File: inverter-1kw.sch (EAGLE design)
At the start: 200 parts, among them IC1 LMV358MMX, IC2 LMV358MMX, U1 ACS712, U4 ACS712, U5 SI8230, U6 SI8230, U7 ACS712, X1 GMSTBV3, X2 MSTBV2

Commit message: Driver ve filtre devresi yerleşimleri yapıldı.
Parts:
- removed C33, C40: (no value), rcl:CPOL-EUE7.5-18
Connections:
- net AGND: no longer C33.-, C40.-
- net VSUPPLY+: no longer C33.+, C40.+

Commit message: Test padler eklendi. Kart destek noktalariyla toprak arasina kondansatorler eklendi.
Cin desarji icin kullanilacak direnc icin 4adet 1206 eklendi.
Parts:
- added C33, C40, C75, C76: 100n, rcl:C-EUC0805
- added R41, R42, R43: (no value), rcl:R-EU_R1206
- added R44: 0R, rcl:R-EU_R1206
- added TP1, TP17, TP18, TP2, TP3, TP4: TPTP17R, testpad:TPTP17R
- added TP10, TP11, TP12, TP13, TP14, TP15, TP16, TP19, TP20, TP21, TP22, TP23, TP24, TP25, TP26, TP27, TP28, TP29, TP30, TP31, TP32, TP33, TP34, TP5, TP6, TP7, TP8, TP9: TPTP06R, testpad:TPTP06R
- R28: device rcl:R-EU_0411/12 -> rcl:R-EU_R1206
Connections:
- new net N$40: C33.2, H1.MOUNT
- new net N$41: C40.2, H2.MOUNT
- new net N$42: C75.1, H3.MOUNT
- new net N$43: C76.1, H4.MOUNT
- new net SUPPLY+: R3.1
- net AGND: now also R41.1, R42.1, R43.1, R44.1, TP10.TP, TP3.TP, TP4.TP, TP9.TP
- net DGND: now also R44.2, TP15.TP, TP16.TP, TP26.TP, TP34.TP
- net G11_PWM: now also TP11.TP
- net G12_PWM: now also TP12.TP
- net G13_PWM: now also TP13.TP
- net G14_PWM: now also TP14.TP
- net IA_SENS: now also TP30.TP
- net IB_SENS: now also TP31.TP
- net IIN_SENS: now also TP33.TP
- net N$20: now also TP23.TP
- net N$23: now also TP24.TP
- net N$35: now also TP5.TP
- net N$37: now also TP7.TP
- net N$7: now also TP19.TP
- net N$75: now also TP6.TP
- net N$81: now also TP8.TP
- net N$9: now also TP20.TP
- net PE: now also C33.1, C40.1, C75.2, C76.2; no longer H1.MOUNT, H2.MOUNT, H3.MOUNT, H4.MOUNT
- net SW_LEG_A: now also TP1.TP, TP28.TP
- net SW_LEG_B: now also TP2.TP
- net VA_OUT: now also TP17.TP
- net VB_OUT: now also TP18.TP
- net VG1_M: now also TP29.TP
- net VG1_P: now also TP27.TP
- net VIN: no longer R3.1
- net VIN_SENS: now also TP32.TP
- net VIN_SENS_DIFF: now also TP21.TP
- net VOUT_SENS_DIFF: now also TP25.TP
- net VREF: now also TP22.TP
- net VSUPPLY+: now also R41.2, R42.2, R43.2

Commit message: bağlantıların bir kısmı yapıldı.
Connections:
- net +3V3: now also SV2.8; no longer SV2.7
- net AGND: now also X1-2.1; no longer X1-3.1
- net DGND: now also SV2.7; no longer SV2.8
- net VSUPPLY+: now also X1-3.1; no longer X1-2.1
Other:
- moved on the sheet: R96, X1-1, X1-2, X1-3
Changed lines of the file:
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@@
 <sheet>
 <plain>
-<wire x1="2.54" y1="-66.04" x2="259.08" y2="-66.04" width="0.6096" layer="125" style="longdash"/>
-<wire x1="259.08" y1="-66.04" x2="260.35" y2="-194.31" width="0.6096" layer="125" style="longdash"/>
+<wire x1="2.54" y1="-66.04" x2="260.35" y2="-66.04" width="0.6096" layer="125" style="longdash"/>
+<wire x1="260.35" y1="-66.04" x2="260.35" y2="-194.31" width="0.6096" layer="125" style="longdash"/>
 <wire x1="260.35" y1="-194.31" x2="3.81" y2="-194.31" width="0.6096" layer="125" style="longdash"/>
 <wire x1="3.81" y1="-194.31" x2="2.54" y2="-66.04" width="0.6096" layer="125" style="longdash"/>
@@
 <attribute name="VALUE" x="298.45" y="-128.27" size="1.778" layer="96" rot="R270"/>
 </instance>
-<instance part="+3V2" gate="G$1" x="300.99" y="-130.81" smashed="yes" rot="R180">
-<attribute name="VALUE" x="303.53" y="-125.73" size="1.778" layer="96" rot="R270"/>
+<instance part="+3V2" gate="G$1" x="303.53" y="-130.81" smashed="yes" rot="R180">
+<attribute name="VALUE" x="306.07" y="-125.73" size="1.778" layer="96" rot="R270"/>
 </instance>
-<instance part="SUPPLY8" gate="G$1" x="303.53" y="-129.54" smashed="yes">
-<attribute name="VALUE" x="300.863" y="-132.715" size="1.778" layer="96"/>
+<instance part="SUPPLY8" gate="G$1" x="300.99" y="-129.54" smashed="yes">
+<attribute name="VALUE" x="298.323" y="-132.715" size="1.778" layer="96"/>
 </instance>
 <instance part="U1" gate="U1" x="669.29" y="50.8" smashed="yes" rot="R90">
@@
 <attribute name="VALUE" x="127.762" y="234.95" size="1.778" layer="96" rot="R90"/>
 </instance>
-<instance part="R96" gate="G$1" x="124.46" y="218.44" smashed="yes" rot="R90">
-<attribute name="NAME" x="122.9614" y="214.63" size="1.778" layer="95" rot="R90"/>
-<attribute name="VALUE" x="127.762" y="214.63" size="1.778" layer="96" rot="R90"/>
+<instance part="R96" gate="G$1" x="124.46" y="217.17" smashed="yes" rot="R90">
+<attribute name="NAME" x="122.9614" y="213.36" size="1.778" layer="95" rot="R90"/>
+<attribute name="VALUE" x="127.762" y="213.36" size="1.778" layer="96" rot="R90"/>
 </instance>
 <instance part="AGND5" gate="VR1" x="746.76" y="71.12" smashed="yes" rot="R180">
@@
 <attribute name="VALUE" x="426.6438" y="-83.566" size="1.778" layer="96" rot="R90"/>
 </instance>
-<instance part="X1" gate="-1" x="6.35" y="-40.64" smashed="yes">
-<attribute name="NAME" x="1.27" y="-39.751" size="1.778" layer="95" rot="R180"/>
+<instance part="X1" gate="-1" x="8.89" y="-39.37" smashed="yes">
+<attribute name="NAME" x="3.81" y="-38.481" size="1.778" layer="95" rot="R180"/>
 </instance>
-<instance part="X1" gate="-2" x="6.35" y="368.3" smashed="yes">
-<attribute name="NAME" x="1.27" y="369.189" size="1.778" layer="95" rot="R180"/>
+<instance part="X1" gate="-2" x="8.89" y="-27.94" smashed="yes">
+<attribute name="NAME" x="3.81" y="-27.051" size="1.778" layer="95" rot="R180"/>
 </instance>
-<instance part="X1" gate="-3" x="6.35" y="-27.94" smashed="yes">
-<attribute name="NAME" x="1.016" y="-27.051" size="1.778" layer="95" rot="R180"/>
-<attribute name="VALUE" x="0" y="-31.75" size="1.778" layer="96"/>
+<instance part="X1" gate="-3" x="6.35" y="368.3" smashed="yes">
+<attribute name="NAME" x="1.016" y="369.189" size="1.778" layer="95" rot="R180"/>
+<attribute name="VALUE" x="0" y="364.49" size="1.778" layer="96"/>
 </instance>
 <instance part="X2" gate="-1" x="815.34" y="224.79" smashed="yes" rot="R180">
@@
 <attribute name="NAME" x="823.214" y="37.211" size="1.778" layer="95"/>
 </instance>
-<instance part="PE1" gate="M" x="13.97" y="-45.72" smashed="yes">
-<attribute name="VALUE" x="11.43" y="-48.26" size="1.778" layer="96" rot="R90"/>
+<instance part="PE1" gate="M" x="16.51" y="-44.45" smashed="yes">
+<attribute name="VALUE" x="13.97" y="-46.99" size="1.778" layer="96" rot="R90"/>
 </instance>
 <instance part="PE2" gate="M" x="414.02" y="-104.14" smashed="yes">
@@
 <segment>
 <pinref part="SUPPLY8" gate="G$1" pin="DGND"/>
-<wire x1="303.53" y1="-127" x2="303.53" y2="-116.84" width="0.1524" layer="91"/>
-<label x="303.53" y="-127" size="1.778" layer="95" rot="R90"/>
-<pinref part="SV2" gate="G$1" pin="8"/>
+<wire x1="300.99" y1="-127" x2="300.99" y2="-116.84" width="0.1524" layer="91"/>
+<label x="300.99" y="-127" size="1.778" layer="95" rot="R90"/>
+<pinref part="SV2" gate="G$1" pin="7"/>
 </segment>
 <segment>
@@
 <segment>
 <pinref part="+3V2" gate="G$1" pin="+3V3"/>
-<wire x1="300.99" y1="-128.27" x2="300.99" y2="-116.84" width="0.1524" layer="91"/>
-<label x="303.53" y="-130.81" size="1.778" layer="95" rot="R180"/>
-<pinref part="SV2" gate="G$1" pin="7"/>
-<label x="300.99" y="-127" size="1.778" layer="95" rot="R90"/>
+<wire x1="303.53" y1="-128.27" x2="303.53" y2="-116.84" width="0.1524" layer="91"/>
+<label x="306.07" y="-127" size="1.778" layer="95" rot="R90"/>
+<label x="303.53" y="-127" size="1.778" layer="95" rot="R90"/>
+<pinref part="SV2" gate="G$1" pin="8"/>
 </segment>
 <segment>
@@
 <junction x="48.26" y="-27.94"/>
 <wire x1="48.26" y1="173.99" x2="48.26" y2="-27.94" width="0.6096" layer="91"/>
-<wire x1="48.26" y1="-27.94" x2="11.43" y2="-27.94" width="0.6096" layer="91"/>
+<wire x1="48.26" y1="-27.94" x2="13.97" y2="-27.94" width="0.6096" layer="91"/>
 <pinref part="R96" gate="G$1" pin="1"/>
-<wire x1="124.46" y1="213.36" x2="124.46" y2="-27.94" width="0.1524" layer="91"/>
+<wire x1="124.46" y1="212.09" x2="124.46" y2="-27.94" width="0.1524" layer="91"/>
 <junction x="124.46" y="-27.94"/>
 <pinref part="LED5" gate="G$1" pin="C"/>
@@
 <pinref part="C48" gate="G$1" pin="2"/>
 <pinref part="C49" gate="G$1" pin="2"/>
-<pinref part="X1" gate="-3" pin="1"/>
 <pinref part="C28" gate="G$1" pin="2"/>
 <wire x1="72.39" y1="177.8" x2="72.39" y2="-27.94" width="0.6096" layer="91"/>
@@
 <wire x1="36.83" y1="173.99" x2="40.64" y2="173.99" width="0.1524" layer="91"/>
 <junction x="40.64" y="173.99"/>
+<pinref part="X1" gate="-2" pin="1"/>
 </segment>
 <segment>
@@
 <junction x="124.46" y="368.3"/>
 <wire x1="48.26" y1="186.69" x2="48.26" y2="187.96" width="0.1524" layer="91"/>
-<pinref part="X1" gate="-2" pin="1"/>
 <pinref part="C28" gate="G$1" pin="1"/>
 <wire x1="72.39" y1="185.42" x2="72.39" y2="368.3" width="0.6096" layer="91"/>
@@
 <wire x1="36.83" y1="189.23" x2="40.64" y2="189.23" width="0.1524" layer="91"/>
 <junction x="40.64" y="189.23"/>
+<pinref part="X1" gate="-3" pin="1"/>
 </segment>
 </net>
@@
 <pinref part="R96" gate="G$1" pin="2"/>
 <wire x1="124.46" y1="233.68" x2="124.46" y2="228.6" width="0.1524" layer="91"/>
-<wire x1="124.46" y1="228.6" x2="124.46" y2="223.52" width="0.1524" layer="91"/>
+<wire x1="124.46" y1="228.6" x2="124.46" y2="222.25" width="0.1524" layer="91"/>
 <wire x1="124.46" y1="228.6" x2="138.43" y2="228.6" width="0.1524" layer="91"/>
 <junction x="124.46" y="228.6"/>
@@
 <segment>
 <pinref part="PE1" gate="M" pin="PE"/>
-<wire x1="13.97" y1="-40.64" x2="13.97" y2="-43.18" width="0.1524" layer="91"/>
-<label x="12.7" y="-49.53" size="1.778" layer="95"/>
+<wire x1="16.51" y1="-39.37" x2="16.51" y2="-41.91" width="0.1524" layer="91"/>
+<label x="15.24" y="-48.26" size="1.778" layer="95"/>
 <pinref part="X1" gate="-1" pin="1"/>
-<wire x1="11.43" y1="-40.64" x2="13.97" y2="-40.64" width="0.1524" layer="91"/>
+<wire x1="13.97" y1="-39.37" x2="16.51" y2="-39.37" width="0.1524" layer="91"/>
 </segment>
 <segment>

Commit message: Planeler yapıldı
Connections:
- net VIN_SENS_DIFF: now also SV1.6; no longer SV1.10
- net VOUT_SENS_DIFF: now also SV1.10; no longer SV1.6
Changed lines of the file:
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@@
 <layer number="131" name="tAdjust" color="7" fill="1" visible="yes" active="yes"/>
 <layer number="132" name="bAdjust" color="7" fill="1" visible="yes" active="yes"/>
+<layer number="133" name="bottom_silk" color="7" fill="1" visible="yes" active="yes"/>
 <layer number="144" name="Drill_legend" color="7" fill="1" visible="yes" active="yes"/>
 <layer number="145" name="DrillLegend_01-02" color="7" fill="1" visible="yes" active="yes"/>
@@
 <sheets>
 <sheet>
+<description>fdkjkldjhjh</description>
 <plain>
 <wire x1="2.54" y1="-66.04" x2="260.35" y2="-66.04" width="0.6096" layer="125" style="longdash"/>
@@
 </segment>
 <segment>
-<pinref part="SV1" gate="G$1" pin="10"/>
-<wire x1="345.44" y1="-119.38" x2="345.44" y2="-130.81" width="0.1524" layer="91"/>
-<label x="345.44" y="-138.43" size="1.778" layer="95" rot="R90"/>
+<wire x1="340.36" y1="-119.38" x2="340.36" y2="-130.81" width="0.1524" layer="91"/>
+<label x="340.36" y="-138.43" size="1.778" layer="95" rot="R90"/>
+<pinref part="SV1" gate="G$1" pin="6"/>
 </segment>
 </net>
@@
 </segment>
 <segment>
-<pinref part="SV1" gate="G$1" pin="6"/>
-<wire x1="340.36" y1="-119.38" x2="340.36" y2="-130.81" width="0.1524" layer="91"/>
-<label x="340.36" y="-140.97" size="1.778" layer="95" rot="R90"/>
+<label x="345.44" y="-140.97" size="1.778" layer="95" rot="R90"/>
+<wire x1="345.44" y1="-119.38" x2="345.44" y2="-130.81" width="0.1524" layer="91"/>
+<pinref part="SV1" gate="G$1" pin="10"/>
 </segment>
 </net>

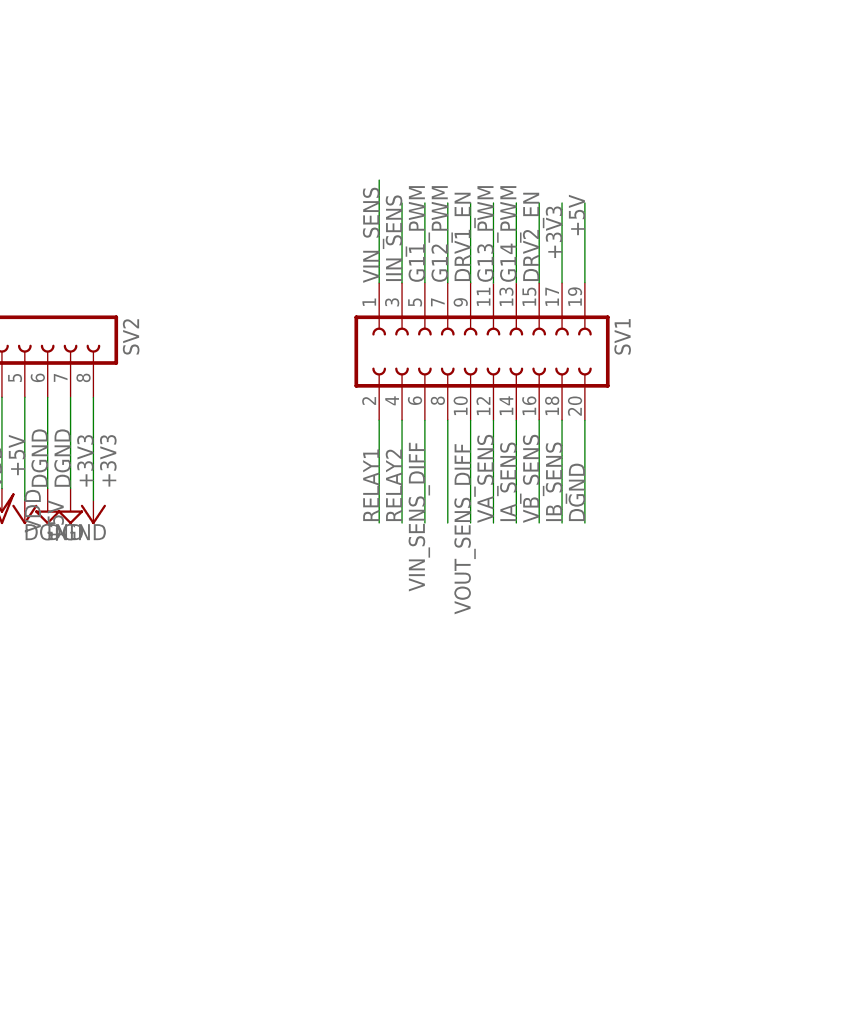
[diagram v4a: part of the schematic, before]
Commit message: Kontrol karti soketi SMD yapildi, guc giris soketi ve guc-karti soketi bottom-layer'a alindi.
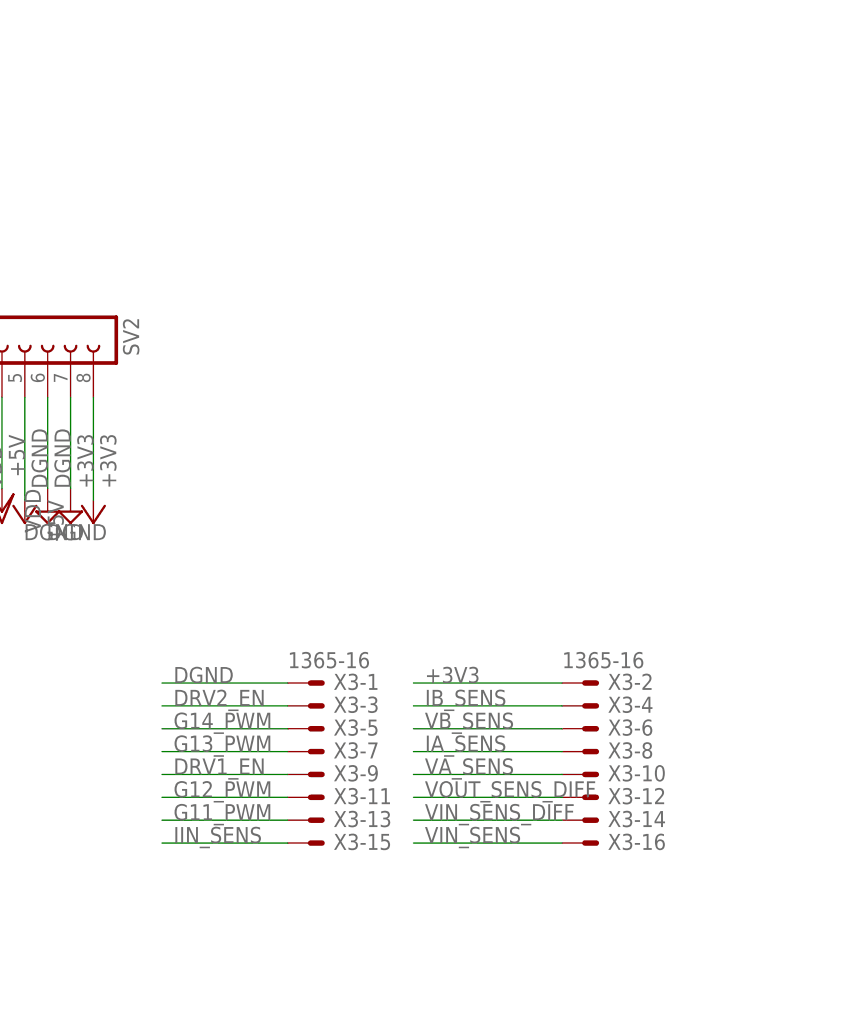
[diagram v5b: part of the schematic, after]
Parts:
- removed SV1: (no value), con-lsta:FE10-2
- added X3: 1365-16, con-leotronics:1365-16
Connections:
- removed net N$38: SV1.8
- removed net RELAY1: SV1.2
- removed net RELAY2: SV1.4
- net +3V3: now also X3-2.S; no longer SV1.17
- net +5V: no longer SV1.19
- net DGND: now also X3-1.S; no longer SV1.20
- net DRV1_EN: now also X3-9.S; no longer SV1.9
- net DRV2_EN: now also X3-3.S; no longer SV1.15
- net G11_PWM: now also X3-13.S; no longer SV1.5
- net G12_PWM: now also X3-11.S; no longer SV1.7
- net G13_PWM: now also X3-7.S; no longer SV1.11
- net G14_PWM: now also X3-5.S; no longer SV1.13
- net IA_SENS: now also X3-8.S; no longer SV1.14
- net IB_SENS: now also X3-4.S; no longer SV1.18
- net IIN_SENS: now also X3-15.S; no longer SV1.3
- net VA_SENS: now also X3-10.S; no longer SV1.12
- net VB_SENS: now also X3-6.S; no longer SV1.16
- net VIN_SENS: now also X3-16.S; no longer SV1.1
- net VIN_SENS_DIFF: now also X3-14.S; no longer SV1.6
- net VOUT_SENS_DIFF: now also X3-12.S; no longer SV1.10

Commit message: Planeler tamamlandı.
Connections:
- net PE: now also X1-3.1; no longer X1-1.1
- net VSUPPLY+: now also X1-1.1; no longer X1-3.1
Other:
- moved on the sheet: X1-1, X1-3
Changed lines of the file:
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@@
 <attribute name="VALUE" x="426.6438" y="-83.566" size="1.778" layer="96" rot="R90"/>
 </instance>
-<instance part="X1" gate="-1" x="8.89" y="-39.37" smashed="yes">
-<attribute name="NAME" x="3.81" y="-38.481" size="1.778" layer="95" rot="R180"/>
+<instance part="X1" gate="-1" x="8.89" y="368.3" smashed="yes">
+<attribute name="NAME" x="3.81" y="369.189" size="1.778" layer="95" rot="R180"/>
 </instance>
 <instance part="X1" gate="-2" x="8.89" y="-27.94" smashed="yes">
 <attribute name="NAME" x="3.81" y="-27.051" size="1.778" layer="95" rot="R180"/>
 </instance>
-<instance part="X1" gate="-3" x="6.35" y="368.3" smashed="yes">
-<attribute name="NAME" x="1.016" y="369.189" size="1.778" layer="95" rot="R180"/>
-<attribute name="VALUE" x="0" y="364.49" size="1.778" layer="96"/>
+<instance part="X1" gate="-3" x="10.16" y="-39.37" smashed="yes">
+<attribute name="NAME" x="4.826" y="-38.481" size="1.778" layer="95" rot="R180"/>
+<attribute name="VALUE" x="3.81" y="-43.18" size="1.778" layer="96"/>
 </instance>
 <instance part="X2" gate="-1" x="815.34" y="224.79" smashed="yes" rot="R180">
@@
 <segment>
 <label x="12.7" y="369.57" size="1.4224" layer="95"/>
-<wire x1="11.43" y1="368.3" x2="48.26" y2="368.3" width="0.6096" layer="91"/>
+<wire x1="13.97" y1="368.3" x2="48.26" y2="368.3" width="0.6096" layer="91"/>
 <wire x1="52.07" y1="185.42" x2="52.07" y2="368.3" width="0.6096" layer="91"/>
 <wire x1="52.07" y1="368.3" x2="59.69" y2="368.3" width="0.6096" layer="91"/>
@@
 <wire x1="36.83" y1="189.23" x2="40.64" y2="189.23" width="0.1524" layer="91"/>
 <junction x="40.64" y="189.23"/>
-<pinref part="X1" gate="-3" pin="1"/>
+<pinref part="X1" gate="-1" pin="1"/>
 </segment>
 </net>
@@
 <wire x1="16.51" y1="-39.37" x2="16.51" y2="-41.91" width="0.1524" layer="91"/>
 <label x="15.24" y="-48.26" size="1.778" layer="95"/>
-<pinref part="X1" gate="-1" pin="1"/>
-<wire x1="13.97" y1="-39.37" x2="16.51" y2="-39.37" width="0.1524" layer="91"/>
-</segment>
-<segment>
+<pinref part="X1" gate="-3" pin="1"/>
+<wire x1="16.51" y1="-39.37" x2="15.24" y2="-39.37" width="0.1524" layer="91"/>
+</segment>
+<segment>

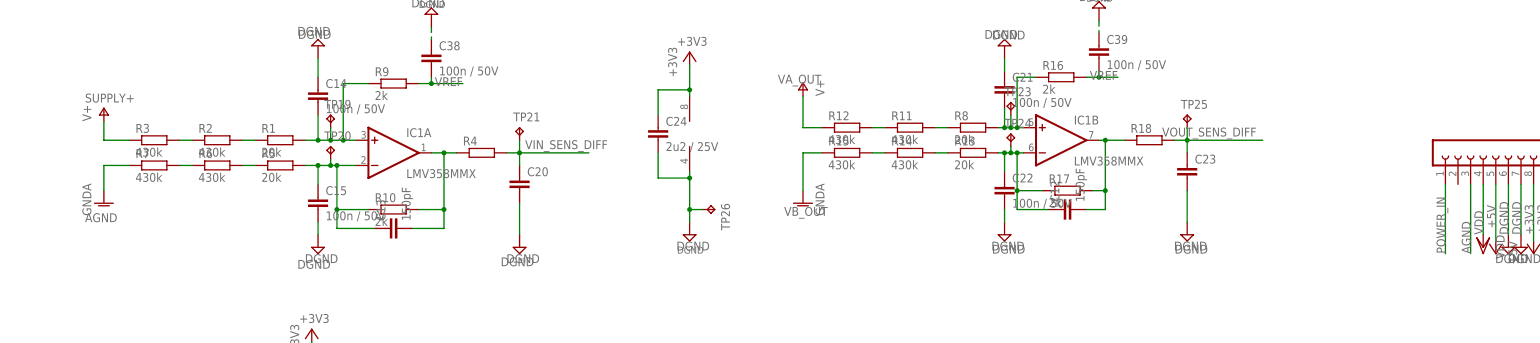
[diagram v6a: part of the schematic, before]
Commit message: R3'un eksik baglantisi yapildi. 8'li besleme karti giris gerilimi baglantisi yapildi.
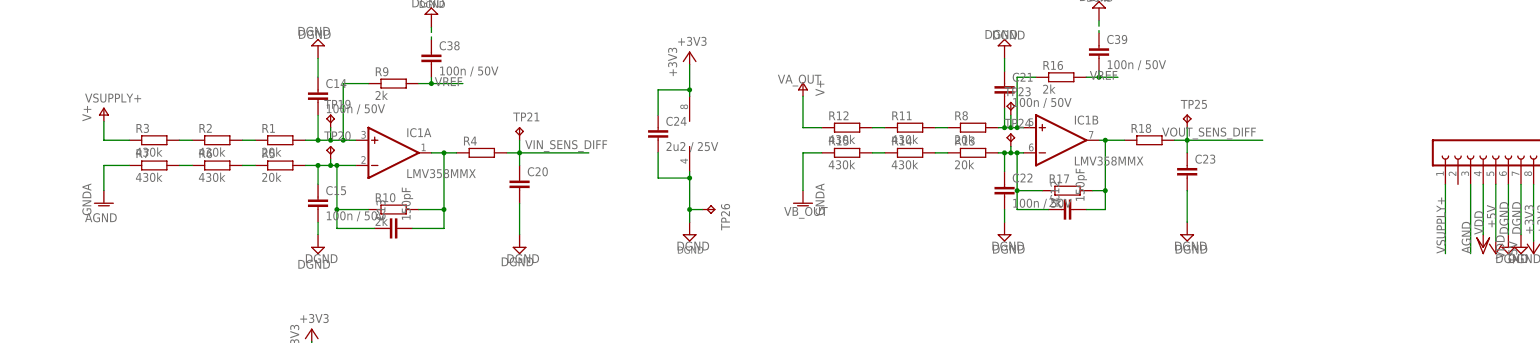
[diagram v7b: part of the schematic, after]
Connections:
- removed net POWER_IN: SV2.1
- removed net SUPPLY+: R3.1
- net VSUPPLY+: now also R3.1, SV2.1
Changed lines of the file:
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@@
 <pinref part="X1" gate="-1" pin="1"/>
+</segment>
+<segment>
+<pinref part="R3" gate="G$1" pin="1"/>
+<wire x1="20.32" y1="-107.95" x2="15.24" y2="-107.95" width="0.1524" layer="91"/>
+<pinref part="P+4" gate="1" pin="V+"/>
+<wire x1="15.24" y1="-104.14" x2="15.24" y2="-107.95" width="0.1524" layer="91"/>
+<label x="11.43" y="-100.33" size="1.778" layer="95"/>
+</segment>
+<segment>
+<wire x1="285.75" y1="-116.84" x2="285.75" y2="-130.81" width="0.1524" layer="91"/>
+<label x="285.75" y="-130.81" size="1.778" layer="95" rot="R90"/>
+<pinref part="SV2" gate="G$1" pin="1"/>
 </segment>
 </net>
@@
 <wire x1="355.6" y1="-161.29" x2="339.09" y2="-161.29" width="0.1524" layer="91"/>
 <label x="340.36" y="-161.29" size="1.778" layer="95"/>
-</segment>
-</net>
-<net name="POWER_IN" class="0">
-<segment>
-<wire x1="285.75" y1="-116.84" x2="285.75" y2="-130.81" width="0.1524" layer="91"/>
-<label x="285.75" y="-130.81" size="1.778" layer="95" rot="R90"/>
-<pinref part="SV2" gate="G$1" pin="1"/>
 </segment>
 </net>
@@
 </segment>
 </net>
-<net name="SUPPLY+" class="0">
-<segment>
-<pinref part="R3" gate="G$1" pin="1"/>
-<wire x1="20.32" y1="-107.95" x2="15.24" y2="-107.95" width="0.1524" layer="91"/>
-<pinref part="P+4" gate="1" pin="V+"/>
-<wire x1="15.24" y1="-104.14" x2="15.24" y2="-107.95" width="0.1524" layer="91"/>
-<label x="11.43" y="-100.33" size="1.778" layer="95"/>
-</segment>
-</net>
